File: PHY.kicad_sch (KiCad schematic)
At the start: 28 parts, among them U13 LAN8742A, Y3 25Mhz

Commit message: change design
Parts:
- C45, C46, C50: value 100n -> 0.1μF
- C52: value 1u -> 1μF
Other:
- moved on the sheet: C46, C50, FB3
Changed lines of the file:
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@@
 	)
 	(junction
-		(at 135.89 82.55)
-		(diameter 0)
-		(color 0 0 0 0)
-	)
-	(junction
 		(at 121.92 87.63)
 		(diameter 0)
@@
 	)
 	(junction
+		(at 132.08 82.55)
+		(diameter 0)
+		(color 0 0 0 0)
+	)
+	(junction
 		(at 102.87 82.55)
 		(diameter 0)
@@
 	)
 	(junction
-		(at 152.4 83.82)
+		(at 154.94 82.55)
 		(diameter 0)
 		(color 0 0 0 0)
@@
 	(wire
 		(pts
-			(xy 121.92 87.63) (xy 135.89 87.63)
+			(xy 121.92 87.63) (xy 132.08 87.63)
+		)
+		(stroke
+			(width 0)
+			(type default)
+		)
+	)
+	(wire
+		(pts
+			(xy 138.43 76.2) (xy 138.43 82.55)
 		)
 		(stroke
@@
 	(wire
 		(pts
-			(xy 135.89 82.55) (xy 138.43 82.55)
-		)
-		(stroke
-			(width 0)
-			(type default)
-		)
-	)
-	(wire
-		(pts
 			(xy 138.43 60.96) (xy 138.43 58.42)
 		)
@@
 	(wire
 		(pts
-			(xy 146.05 91.44) (xy 146.05 83.82)
+			(xy 146.05 91.44) (xy 146.05 82.55)
 		)
 		(stroke
@@
 	(wire
 		(pts
-			(xy 121.92 82.55) (xy 135.89 82.55)
+			(xy 121.92 82.55) (xy 132.08 82.55)
 		)
 		(stroke
@@
 	(wire
 		(pts
+			(xy 132.08 82.55) (xy 138.43 82.55)
+		)
+		(stroke
+			(width 0)
+			(type default)
+		)
+	)
+	(wire
+		(pts
 			(xy 102.87 129.54) (xy 123.19 129.54)
 		)
@@
 	(wire
 		(pts
-			(xy 138.43 74.93) (xy 138.43 60.96)
+			(xy 138.43 68.58) (xy 138.43 60.96)
 		)
 		(stroke
@@
 	(wire
 		(pts
-			(xy 146.05 83.82) (xy 152.4 83.82)
+			(xy 146.05 82.55) (xy 154.94 82.55)
 		)
 		(stroke
@@
 		(shape input)
 		(at 78.74 116.84 180)
-		(fields_autoplaced yes)
 		(effects
 			(font
@@
 		(shape output)
 		(at 217.17 121.92 0)
-		(fields_autoplaced yes)
 		(effects
 			(font
@@
 		(shape output)
 		(at 78.74 109.22 180)
-		(fields_autoplaced yes)
 		(effects
 			(font
@@
 		(shape input)
 		(at 78.74 114.3 180)
-		(fields_autoplaced yes)
 		(effects
 			(font
@@
 		(shape output)
 		(at 217.17 134.62 0)
-		(fields_autoplaced yes)
 		(effects
 			(font
@@
 		(shape input)
 		(at 217.17 106.68 0)
-		(fields_autoplaced yes)
 		(effects
 			(font
@@
 		(shape output)
 		(at 217.17 116.84 0)
-		(fields_autoplaced yes)
 		(effects
 			(font
@@
 		(shape input)
 		(at 217.17 109.22 0)
-		(fields_autoplaced yes)
 		(effects
 			(font
@@
 		(shape input)
 		(at 217.17 127 0)
-		(fields_autoplaced yes)
 		(effects
 			(font
@@
 		(shape input)
 		(at 217.17 132.08 0)
-		(fields_autoplaced yes)
 		(effects
 			(font
@@
 		(shape output)
 		(at 217.17 114.3 0)
-		(fields_autoplaced yes)
 		(effects
 			(font
@@
 		(shape input)
 		(at 217.17 111.76 0)
-		(fields_autoplaced yes)
 		(effects
 			(font
@@
 		(shape bidirectional)
 		(at 217.17 124.46 0)
-		(fields_autoplaced yes)
 		(effects
 			(font
@@
 		(shape output)
 		(at 78.74 111.76 180)
-		(fields_autoplaced yes)
 		(effects
 			(font
@@
 	(symbol
 		(lib_id "Device:C_Small")
-		(at 152.4 86.36 0)
+		(at 154.94 85.09 0)
 		(mirror y)
 		(unit 1)
@@
 		(dnp no)
 		(property "Reference" "C46"
-			(at 150.0632 85.1916 0)
+			(at 152.6032 83.9216 0)
 			(effects
 				(font
@@
 			)
 		)
-		(property "Value" "100n"
-			(at 150.0632 87.503 0)
+		(property "Value" "0.1μF"
+			(at 152.6032 86.233 0)
 			(effects
 				(font
@@
 		)
 		(property "Footprint" "Capacitor_SMD:C_0603_1608Metric_Pad1.08x0.95mm_HandSolder"
-			(at 152.4 86.36 0)
+			(at 154.94 85.09 0)
 			(effects
 				(font
@@
 		)
 		(property "Datasheet" "~"
-			(at 152.4 86.36 0)
+			(at 154.94 85.09 0)
 			(effects
 				(font
@@
 		)
 		(property "Description" ""
-			(at 152.4 86.36 0)
+			(at 154.94 85.09 0)
 			(effects
 				(font
@@
 		)
 		(property "DESCRIPTION" "Capacitor 100n 0603"
-			(at 152.4 86.36 0)
+			(at 154.94 85.09 0)
 			(effects
 				(font
@@
 		)
 		(property "MANUFACTURER_PART_NUMBER" "CC0603KRX7R9BB104"
-			(at 152.4 86.36 0)
+			(at 154.94 85.09 0)
 			(effects
 				(font
@@
 		)
 		(property "MANUFACTURER" "Yageo"
-			(at 152.4 86.36 0)
+			(at 154.94 85.09 0)
 			(effects
 				(font
@@
 	(symbol
 		(lib_id "Device:C_Small")
-		(at 135.89 85.09 0)
+		(at 132.08 85.09 0)
 		(mirror y)
 		(unit 1)
@@
 		(dnp no)
 		(property "Reference" "C50"
-			(at 133.5532 83.9216 0)
+			(at 129.7432 83.9216 0)
 			(effects
 				(font
@@
 			)
 		)
-		(property "Value" "100n"
-			(at 133.5532 86.233 0)
+		(property "Value" "0.1μF"
+			(at 129.7432 86.233 0)
 			(effects
 				(font
@@
 		)
 		(property "Footprint" "Capacitor_SMD:C_0603_1608Metric_Pad1.08x0.95mm_HandSolder"
-			(at 135.89 85.09 0)
+			(at 132.08 85.09 0)
 			(effects
 				(font
@@
 		)
 		(property "Datasheet" "~"
-			(at 135.89 85.09 0)
+			(at 132.08 85.09 0)
 			(effects
 				(font
@@
 		)
 		(property "Description" ""
-			(at 135.89 85.09 0)
+			(at 132.08 85.09 0)
 			(effects
 				(font
@@
 		)
 		(property "DESCRIPTION" "Capacitor 100n 0603"
-			(at 135.89 85.09 0)
+			(at 132.08 85.09 0)
 			(effects
 				(font
@@
 		)
 		(property "MANUFACTURER_PART_NUMBER" "CC0603KRX7R9BB104"
-			(at 135.89 85.09 0)
+			(at 132.08 85.09 0)
 			(effects
 				(font
@@
 		)
 		(property "MANUFACTURER" "Yageo"
-			(at 135.89 85.09 0)
+			(at 132.08 85.09 0)
 			(effects
 				(font
@@
 			)
 		)
-		(property "Value" "1u"
+		(property "Value" "1μF"
 			(at 159.8168 68.453 0)
 			(effects
@@
 	(symbol
 		(lib_id "h730duino-rescue:GND-power")
-		(at 152.4 88.9 0)
+		(at 154.94 87.63 0)
 		(unit 1)
 		(exclude_from_sim no)
@@
 		(dnp no)
 		(property "Reference" "#PWR01204"
-			(at 152.4 95.25 0)
+			(at 154.94 93.98 0)
 			(effects
 				(font
@@
 		)
 		(property "Value" "GND"
-			(at 152.527 93.2942 0)
+			(at 155.067 92.0242 0)
 			(effects
 				(font
@@
 		)
 		(property "Footprint" ""
-			(at 152.4 88.9 0)
+			(at 154.94 87.63 0)
 			(effects
 				(font
@@
 		)
 		(property "Datasheet" ""
-			(at 152.4 88.9 0)
+			(at 154.94 87.63 0)
 			(effects
 				(font
@@
 		)
 		(property "Description" ""
-			(at 152.4 88.9 0)
+			(at 154.94 87.63 0)
 			(effects
 				(font
@@
 	(symbol
 		(lib_id "Device:FerriteBead")
-		(at 138.43 78.74 0)
+		(at 138.43 72.39 0)
 		(unit 1)
 		(exclude_from_sim no)
@@
 		(dnp no)
 		(property "Reference" "FB3"
-			(at 124.206 74.422 0)
+			(at 124.206 68.072 0)
 			(effects
 				(font
@@
 		)
 		(property "Value" "FerriteBead"
-			(at 124.206 76.962 0)
+			(at 124.206 70.612 0)
 			(effects
 				(font
@@
 		)
 		(property "Footprint" "Inductor_SMD:L_0603_1608Metric_Pad1.05x0.95mm_HandSolder"
-			(at 136.652 78.74 90)
+			(at 136.652 72.39 90)
 			(effects
 				(font
@@
 		)
 		(property "Datasheet" "~"
-			(at 138.43 78.74 0)
+			(at 138.43 72.39 0)
 			(effects
 				(font
@@
 		)
 		(property "Description" "Ferrite bead"
-			(at 138.43 78.74 0)
+			(at 138.43 72.39 0)
 			(effects
 				(font
@@
 		(dnp no)
 		(property "Reference" "C45"
-			(at 119.5832 83.9216 0)
+			(at 119.634 84.074 0)
 			(effects
 				(font
@@
 			)
 		)
-		(property "Value" "100n"
-			(at 119.5832 86.233 0)
+		(property "Value" "0.1μF"
+			(at 119.634 86.3854 0)
 			(effects
 				(font
@@
 	(symbol
 		(lib_id "power:+3.3V")
-		(at 152.4 83.82 0)
+		(at 154.94 82.55 0)
 		(unit 1)
 		(exclude_from_sim no)
@@
 		(fields_autoplaced yes)
 		(property "Reference" "#PWR01203"
-			(at 152.4 87.63 0)
+			(at 154.94 86.36 0)
 			(effects
 				(font
@@
 		)
 		(property "Value" "+3.3V"
-			(at 152.4 78.74 0)
+			(at 154.94 77.47 0)
 			(effects
 				(font
@@
 		)
 		(property "Footprint" ""
-			(at 152.4 83.82 0)
+			(at 154.94 82.55 0)
 			(effects
 				(font
@@
 		)
 		(property "Datasheet" ""
-			(at 152.4 83.82 0)
+			(at 154.94 82.55 0)
 			(effects
 				(font
@@
 		)
 		(property "Description" "Power symbol creates a global label with name \"+3.3V\""
-			(at 152.4 83.82 0)
+			(at 154.94 82.55 0)
 			(effects
 				(font

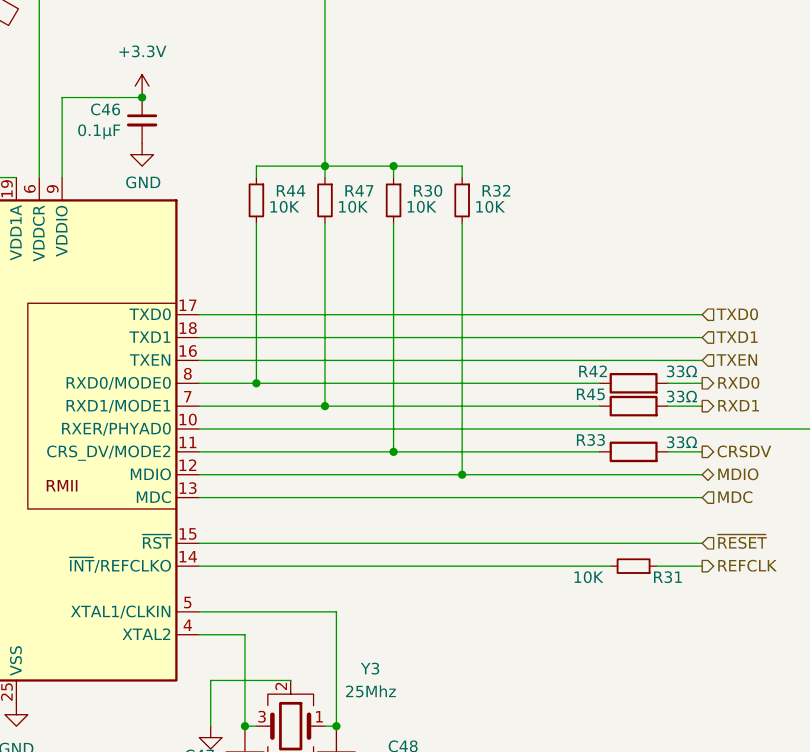
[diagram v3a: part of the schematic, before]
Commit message: add capacitor
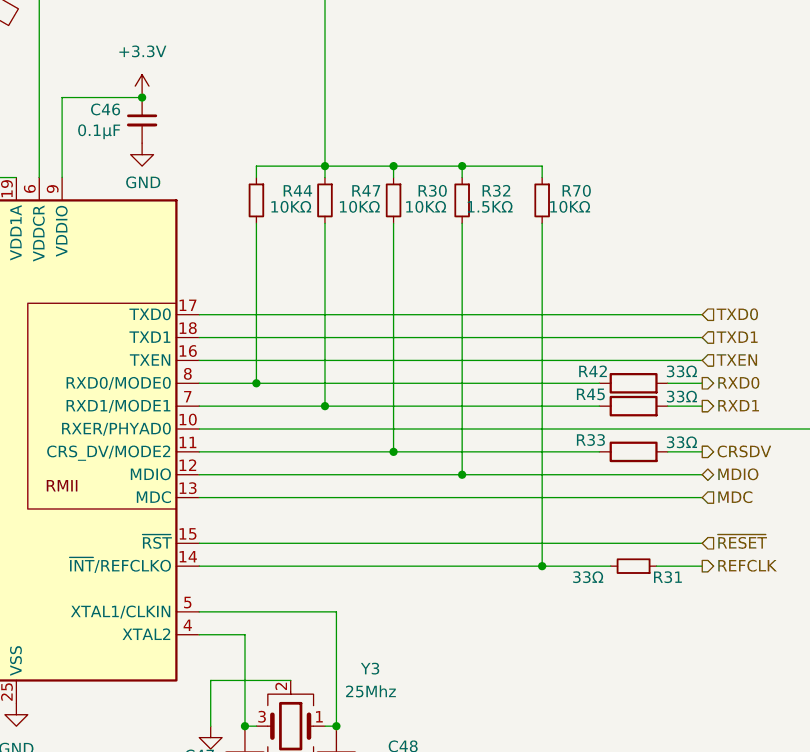
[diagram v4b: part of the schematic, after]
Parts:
- added R70: 10KΩ, Resistor_SMD:R_0603_1608Metric_Pad0.98x0.95mm_HandSolder, symbol Device:R_Small
- C45, C46, C50: footprint Capacitor_SMD:C_0603_1608Metric_Pad1.08x0.95mm_HandSolder -> Capacitor_SMD:C_0402_1005Metric_Pad0.74x0.62mm_HandSolder
- R30, R44, R47: value 10K -> 10KΩ
- R31: value 10K -> 33Ω
- R32: value 10K -> 1.5KΩ
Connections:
- net +3.3V: now also R70.1
- net at R31.2, U13.14 (~{INT}/REFCLKO): now also R70.2
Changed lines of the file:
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@@
 	)
 	(junction
+		(at 199.39 134.62)
+		(diameter 0)
+		(color 0 0 0 0)
+	)
+	(junction
 		(at 157.48 69.85)
 		(diameter 0)
@@
 	)
 	(junction
+		(at 190.5 90.17)
+		(diameter 0)
+		(color 0 0 0 0)
+	)
+	(junction
 		(at 175.26 90.17)
 		(diameter 0)
@@
 	(wire
 		(pts
+			(xy 199.39 90.17) (xy 199.39 91.44)
+		)
+		(stroke
+			(width 0)
+			(type default)
+		)
+	)
+	(wire
+		(pts
 			(xy 171.45 157.48) (xy 171.45 160.02)
 		)
@@
 	(wire
 		(pts
-			(xy 207.01 134.62) (xy 161.29 134.62)
+			(xy 207.01 134.62) (xy 199.39 134.62)
 		)
 		(stroke
@@
 	(wire
 		(pts
+			(xy 199.39 134.62) (xy 161.29 134.62)
+		)
+		(stroke
+			(width 0)
+			(type default)
+		)
+	)
+	(wire
+		(pts
+			(xy 199.39 96.52) (xy 199.39 134.62)
+		)
+		(stroke
+			(width 0)
+			(type default)
+		)
+	)
+	(wire
+		(pts
+			(xy 190.5 90.17) (xy 199.39 90.17)
+		)
+		(stroke
+			(width 0)
+			(type default)
+		)
+	)
+	(wire
+		(pts
 			(xy 121.92 82.55) (xy 132.08 82.55)
 		)
@@
 			)
 		)
-		(property "Footprint" "Capacitor_SMD:C_0603_1608Metric_Pad1.08x0.95mm_HandSolder"
+		(property "Footprint" "Capacitor_SMD:C_0402_1005Metric_Pad0.74x0.62mm_HandSolder"
 			(at 154.94 85.09 0)
 			(effects
@@
 			)
 		)
-		(property "Footprint" "Capacitor_SMD:C_0603_1608Metric_Pad1.08x0.95mm_HandSolder"
+		(property "Footprint" "Capacitor_SMD:C_0402_1005Metric_Pad0.74x0.62mm_HandSolder"
 			(at 132.08 85.09 0)
 			(effects
@@
 		(dnp no)
 		(property "Reference" "R47"
-			(at 179.07 92.964 0)
+			(at 179.832 92.964 0)
 			(effects
 				(font
@@
 			)
 		)
-		(property "Value" "10K"
-			(at 178.308 94.742 0)
+		(property "Value" "10KΩ"
+			(at 179.07 94.742 0)
 			(effects
 				(font
@@
 		(dnp no)
 		(property "Reference" "R44"
-			(at 171.45 92.964 0)
+			(at 172.212 92.964 0)
 			(effects
 				(font
@@
 			)
 		)
-		(property "Value" "10K"
-			(at 170.688 94.742 0)
+		(property "Value" "10KΩ"
+			(at 171.45 94.742 0)
 			(effects
 				(font
@@
 			)
 		)
-		(property "Value" "10K"
+		(property "Value" "1.5KΩ"
 			(at 193.548 94.742 0)
 			(effects
@@
 			)
 		)
-		(property "Value" "10K"
+		(property "Value" "33Ω"
 			(at 204.47 135.89 90)
 			(effects
@@
 		(dnp no)
 		(property "Reference" "R30"
-			(at 186.69 92.964 0)
+			(at 187.198 92.964 0)
 			(effects
 				(font
@@
 			)
 		)
-		(property "Value" "10K"
-			(at 185.928 94.742 0)
+		(property "Value" "10KΩ"
+			(at 186.436 94.742 0)
 			(effects
 				(font
@@
 			)
 		)
-		(property "Footprint" "Capacitor_SMD:C_0603_1608Metric_Pad1.08x0.95mm_HandSolder"
+		(property "Footprint" "Capacitor_SMD:C_0402_1005Metric_Pad0.74x0.62mm_HandSolder"
 			(at 121.92 85.09 0)
 			(effects
@@
 					(unit 1)
 				)
+			)
+		)
+	)
+	(symbol
+		(lib_id "Device:R_Small")
+		(at 199.39 93.98 0)
+		(mirror y)
+		(unit 1)
+		(exclude_from_sim no)
+		(in_bom yes)
+		(on_board yes)
+		(dnp no)
+		(property "Reference" "R70"
+			(at 203.2 92.964 0)
+			(effects
+				(font
+					(size 1.27 1.27)
+				)
+			)
+		)
+		(property "Value" "10KΩ"
+			(at 202.438 94.742 0)
+			(effects
+				(font
+					(size 1.27 1.27)
+				)
+			)
+		)
+		(property "Footprint" "Resistor_SMD:R_0603_1608Metric_Pad0.98x0.95mm_HandSolder"
+			(at 199.39 93.98 0)
+			(effects
+				(font
+					(size 1.27 1.27)
+				)
+				(hide yes)
+			)
+		)
+		(property "Datasheet" "~"
+			(at 199.39 93.98 0)
+			(effects
+				(font
+					(size 1.27 1.27)
+				)
+				(hide yes)
+			)
+		)
+		(property "Description" ""
+			(at 199.39 93.98 0)
+			(effects
+				(font
+					(size 1.27 1.27)
+				)
+				(hide yes)
+			)
+		)
+		(property "DESCRIPTION" "Resistor 10K 0603"
+			(at 199.39 93.98 0)
+			(effects
+				(font
+					(size 1.27 1.27)
+				)
+				(hide yes)
+			)
+		)
+		(property "MANUFACTURER" "Yageo"
+			(at 199.39 93.98 0)
+			(effects
+				(font
+					(size 1.27 1.27)
+				)
+				(hide yes)
+			)
+		)
+		(property "MANUFACTURER_PART_NUMBER" "RC0603FR-0710KL"
+			(at 199.39 93.98 0)
+			(effects
+				(font
+					(size 1.27 1.27)
+				)
+				(hide yes)
+			)
+		)
+		(pin "1"
+		)
+		(pin "2"
+		)
+		(instances
+			(project "mainboard4"
+				(path "/dd07ab80-a59c-44f4-ac7d-849e21e1384e/4fc6aed4-b6ec-46a7-b9d1-1f9060000df7"
+					(reference "R70")
+					(unit 1)
+				)
